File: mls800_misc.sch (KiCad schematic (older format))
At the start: 18 parts, among them SW2 SW_TACT_LED, SW3 SW_TACT_LED, SW4 SW_TACT_LED, SW5 SW_TACT_LED, SW6 SW_TACT_LED, SW7 SW_TACT_LED, SW8 SW_TACT_LED, SW9 SW_TACT_LED, U4 MCP23017

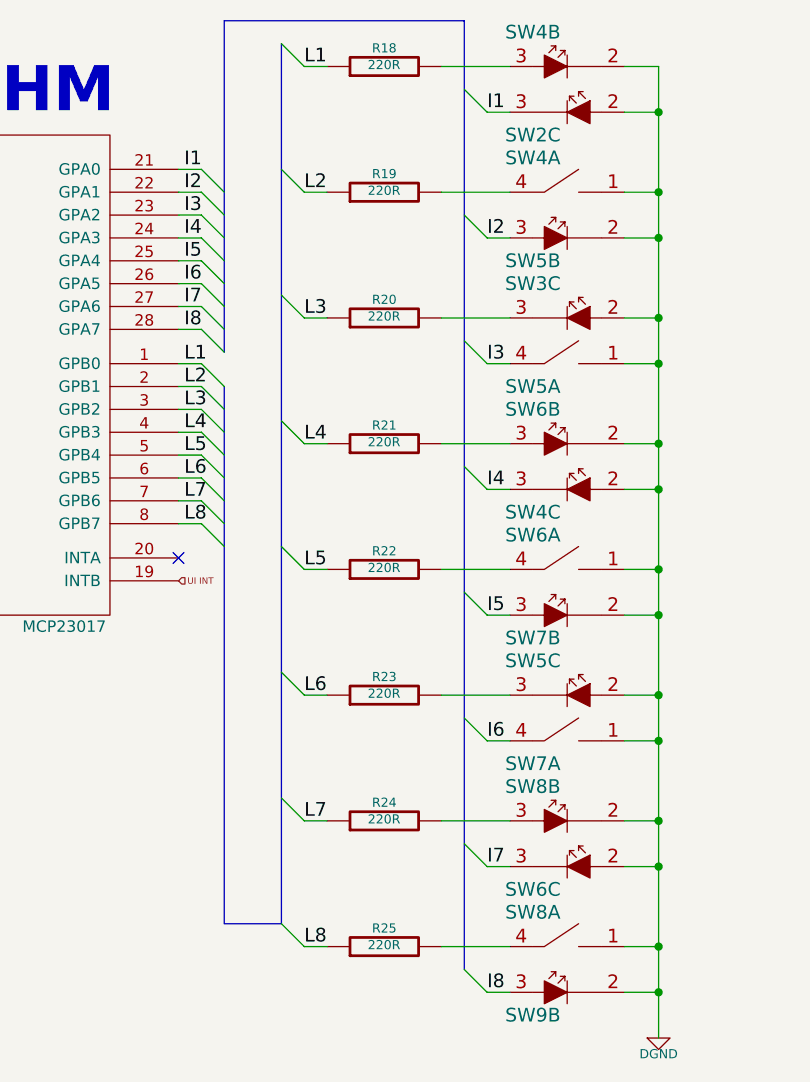
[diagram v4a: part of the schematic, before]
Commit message: MLS800 : disabled switch tact led "interchangeable" units => fixed annotations
MLS800 : fixed some erc errors in old "misc" sheet
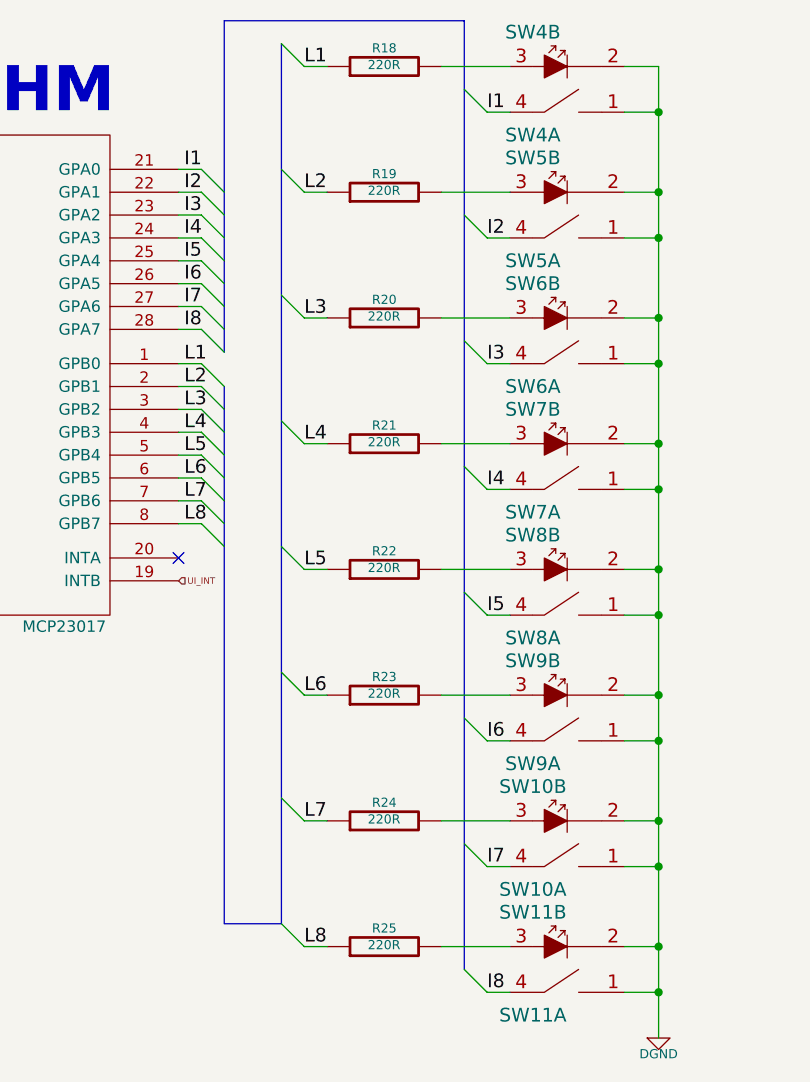
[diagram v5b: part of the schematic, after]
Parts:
- renumbered SW6 to SW10, SW8 to SW10, SW9 to SW11, SW8 to SW11, SW2 to SW4, SW4 to SW5, SW5 to SW6, SW3 to SW6, SW4 to SW7, SW6 to SW7, SW7 to SW8, SW6 to SW8, SW7 to SW9, SW5 to SW9
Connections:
- net DGND: now also SW10.1, SW11.1, SW11.2, SW4.1, SW5.1, SW5.2, SW7.1, SW8.1, SW8.2; no longer SW10.2, SW11.1, SW11.2, SW4.2, SW5.1, SW5.2, SW7.2, SW8.1, SW8.2
- net I1: now also SW4.4; no longer SW4.3
- net I2: now also SW5.4; no longer SW5.3
- net I4: now also SW7.4; no longer SW7.3
- net I5: now also SW8.4; no longer SW8.3
- net I7: now also SW10.4; no longer SW10.3
- net I8: now also SW11.4; no longer SW11.3
- net at R19.2: now also SW5.3; no longer SW5.4
- net at R22.2: now also SW8.3; no longer SW8.4
- net at R25.2: now also SW11.3; no longer SW11.4
- net UI INT renamed UI_INT
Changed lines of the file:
@@
 $EndComp
 $Comp
-L VCC #PWR43
+L VCC #PWR045
 U 1 1 5350562C
 P 750 1500
-F 0 "#PWR43" H 750 1600 30  0001 C CNN
+F 0 "#PWR045" H 750 1600 30  0001 C CNN
 F 1 "VCC" H 750 1600 30  0000 C CNN
 F 2 "" H 750 1500 60  0000 C CNN
@@
 SCL
 Text HLabel 3150 3350 2    28   Input ~ 0
-UI INT
+UI_INT
 NoConn ~ 3150 3250
 Entry Wire Line
@@
 	3600 4850 3700 4950
 $Comp
-L SW_TACT_LED SW2
-U 3 1 53B9BB32
+L SW_TACT_LED SW4
+U 1 1 53B9BB32
 P 4900 1300
-F 0 "SW2" H 4700 1200 60  0000 C CNN
+F 0 "SW4" H 4700 1200 60  0000 C CNN
 F 1 "SW_TACT_LED" H 4950 1200 60  0001 C CNN
 F 2 "" H 4900 1300 60  0000 C CNN
 F 3 "" H 4900 1300 60  0000 C CNN
-	3    4900 1300
+	1    4900 1300
 	1    0    0    -1
 $EndComp
@@
 $Comp
 L SW_TACT_LED SW5
-U 2 1 53B9BB96
+U 1 1 53B9BB96
 P 4900 1850
 F 0 "SW5" H 4700 1750 60  0000 C CNN
@@
 F 2 "" H 4900 1850 60  0000 C CNN
 F 3 "" H 4900 1850 60  0000 C CNN
-	2    4900 1850
-	1    0    0    -1
-$EndComp
-$Comp
-L SW_TACT_LED SW4
-U 1 1 53B9BB9C
+	1    4900 1850
+	1    0    0    -1
+$EndComp
+$Comp
+L SW_TACT_LED SW5
+U 2 1 53B9BB9C
 P 4900 1650
-F 0 "SW4" H 4700 1800 60  0000 C CNN
+F 0 "SW5" H 4700 1800 60  0000 C CNN
 F 1 "SW_TACT_LED" H 4950 1550 60  0001 C CNN
 F 2 "" H 4900 1650 60  0000 C CNN
 F 3 "" H 4900 1650 60  0000 C CNN
-	1    4900 1650
-	1    0    0    -1
-$EndComp
-$Comp
-L SW_TACT_LED SW5
+	2    4900 1650
+	1    0    0    -1
+$EndComp
+$Comp
+L SW_TACT_LED SW6
 U 1 1 53B9BBAC
 P 4900 2400
-F 0 "SW5" H 4700 2300 60  0000 C CNN
+F 0 "SW6" H 4700 2300 60  0000 C CNN
 F 1 "SW_TACT_LED" H 4950 2300 60  0001 C CNN
 F 2 "" H 4900 2400 60  0000 C CNN
@@
 $EndComp
 $Comp
-L SW_TACT_LED SW3
-U 3 1 53B9BBB2
+L SW_TACT_LED SW6
+U 2 1 53B9BBB2
 P 4900 2200
-F 0 "SW3" H 4700 2350 60  0000 C CNN
+F 0 "SW6" H 4700 2350 60  0000 C CNN
 F 1 "SW_TACT_LED" H 4950 2100 60  0001 C CNN
 F 2 "" H 4900 2200 60  0000 C CNN
 F 3 "" H 4900 2200 60  0000 C CNN
-	3    4900 2200
-	1    0    0    -1
-$EndComp
-$Comp
-L SW_TACT_LED SW4
-U 3 1 53B9BBB8
+	2    4900 2200
+	1    0    0    -1
+$EndComp
+$Comp
+L SW_TACT_LED SW7
+U 1 1 53B9BBB8
 P 4900 2950
-F 0 "SW4" H 4700 2850 60  0000 C CNN
+F 0 "SW7" H 4700 2850 60  0000 C CNN
 F 1 "SW_TACT_LED" H 4950 2850 60  0001 C CNN
 F 2 "" H 4900 2950 60  0000 C CNN
 F 3 "" H 4900 2950 60  0000 C CNN
-	3    4900 2950
-	1    0    0    -1
-$EndComp
-$Comp
-L SW_TACT_LED SW6
+	1    4900 2950
+	1    0    0    -1
+$EndComp
+$Comp
+L SW_TACT_LED SW7
 U 2 1 53B9BBBE
 P 4900 2750
-F 0 "SW6" H 4700 2900 60  0000 C CNN
+F 0 "SW7" H 4700 2900 60  0000 C CNN
 F 1 "SW_TACT_LED" H 4950 2650 60  0001 C CNN
 F 2 "" H 4900 2750 60  0000 C CNN
@@
 $EndComp
 $Comp
-L SW_TACT_LED SW7
-U 2 1 53B9BBC4
+L SW_TACT_LED SW8
+U 1 1 53B9BBC4
 P 4900 3500
-F 0 "SW7" H 4700 3400 60  0000 C CNN
+F 0 "SW8" H 4700 3400 60  0000 C CNN
 F 1 "SW_TACT_LED" H 4950 3400 60  0001 C CNN
 F 2 "" H 4900 3500 60  0000 C CNN
 F 3 "" H 4900 3500 60  0000 C CNN
-	2    4900 3500
-	1    0    0    -1
-$EndComp
-$Comp
-L SW_TACT_LED SW6
-U 1 1 53B9BBCA
+	1    4900 3500
+	1    0    0    -1
+$EndComp
+$Comp
+L SW_TACT_LED SW8
+U 2 1 53B9BBCA
 P 4900 3300
-F 0 "SW6" H 4700 3450 60  0000 C CNN
+F 0 "SW8" H 4700 3450 60  0000 C CNN
 F 1 "SW_TACT_LED" H 4950 3200 60  0001 C CNN
 F 2 "" H 4900 3300 60  0000 C CNN
 F 3 "" H 4900 3300 60  0000 C CNN
-	1    4900 3300
-	1    0    0    -1
-$EndComp
-$Comp
-L SW_TACT_LED SW7
+	2    4900 3300
+	1    0    0    -1
+$EndComp
+$Comp
+L SW_TACT_LED SW9
 U 1 1 53B9BBD0
 P 4900 4050
-F 0 "SW7" H 4700 3950 60  0000 C CNN
+F 0 "SW9" H 4700 3950 60  0000 C CNN
 F 1 "SW_TACT_LED" H 4950 3950 60  0001 C CNN
 F 2 "" H 4900 4050 60  0000 C CNN
@@
 $EndComp
 $Comp
-L SW_TACT_LED SW5
-U 3 1 53B9BBD6
+L SW_TACT_LED SW9
+U 2 1 53B9BBD6
 P 4900 3850
-F 0 "SW5" H 4700 4000 60  0000 C CNN
+F 0 "SW9" H 4700 4000 60  0000 C CNN
 F 1 "SW_TACT_LED" H 4950 3750 60  0001 C CNN
 F 2 "" H 4900 3850 60  0000 C CNN
 F 3 "" H 4900 3850 60  0000 C CNN
-	3    4900 3850
-	1    0    0    -1
-$EndComp
-$Comp
-L SW_TACT_LED SW6
-U 3 1 53B9BBDC
+	2    4900 3850
+	1    0    0    -1
+$EndComp
+$Comp
+L SW_TACT_LED SW10
+U 1 1 53B9BBDC
 P 4900 4600
-F 0 "SW6" H 4700 4500 60  0000 C CNN
+F 0 "SW10" H 4700 4500 60  0000 C CNN
 F 1 "SW_TACT_LED" H 4950 4500 60  0001 C CNN
 F 2 "" H 4900 4600 60  0000 C CNN
 F 3 "" H 4900 4600 60  0000 C CNN
-	3    4900 4600
-	1    0    0    -1
-$EndComp
-$Comp
-L SW_TACT_LED SW8
+	1    4900 4600
+	1    0    0    -1
+$EndComp
+$Comp
+L SW_TACT_LED SW10
 U 2 1 53B9BBE2
 P 4900 4400
-F 0 "SW8" H 4700 4550 60  0000 C CNN
+F 0 "SW10" H 4700 4550 60  0000 C CNN
 F 1 "SW_TACT_LED" H 4950 4300 60  0001 C CNN
 F 2 "" H 4900 4400 60  0000 C CNN
@@
 $EndComp
 $Comp
-L SW_TACT_LED SW9
-U 2 1 53B9BBE8
+L SW_TACT_LED SW11
+U 1 1 53B9BBE8
 P 4900 5150
-F 0 "SW9" H 4700 5050 60  0000 C CNN
+F 0 "SW11" H 4700 5050 60  0000 C CNN
 F 1 "SW_TACT_LED" H 4950 5050 60  0001 C CNN
 F 2 "" H 4900 5150 60  0000 C CNN
 F 3 "" H 4900 5150 60  0000 C CNN
-	2    4900 5150
-	1    0    0    -1
-$EndComp
-$Comp
-L SW_TACT_LED SW8
-U 1 1 53B9BBEE
+	1    4900 5150
+	1    0    0    -1
+$EndComp
+$Comp
+L SW_TACT_LED SW11
+U 2 1 53B9BBEE
 P 4900 4950
-F 0 "SW8" H 4700 5100 60  0000 C CNN
+F 0 "SW11" H 4700 5100 60  0000 C CNN
 F 1 "SW_TACT_LED" H 4950 4850 60  0001 C CNN
 F 2 "" H 4900 4950 60  0000 C CNN
 F 3 "" H 4900 4950 60  0000 C CNN
-	1    4900 4950
+	2    4900 4950
 	1    0    0    -1
 $EndComp
@@
 Connection ~ 5250 1300
 $Comp
-L DGND #PWR46
+L DGND #PWR046
 U 1 1 53F19F43
 P 5250 5350
-F 0 "#PWR46" H 5250 5350 40  0001 C CNN
+F 0 "#PWR046" H 5250 5350 40  0001 C CNN
 F 1 "DGND" H 5250 5280 40  0000 C CNN
 F 2 "" H 5250 5350 60  0000 C CNN
@@
 $EndComp
 $Comp
-L DGND #PWR45
+L DGND #PWR047
 U 1 1 53F19F5C
 P 2200 3800
-F 0 "#PWR45" H 2200 3800 40  0001 C CNN
+F 0 "#PWR047" H 2200 3800 40  0001 C CNN
 F 1 "DGND" H 2200 3730 40  0000 C CNN
 F 2 "" H 2200 3800 60  0000 C CNN
@@
 $EndComp
 $Comp
-L DGND #PWR44
+L DGND #PWR048
 U 1 1 53F19F6B
 P 1100 2100
-F 0 "#PWR44" H 1100 2100 40  0001 C CNN
+F 0 "#PWR048" H 1100 2100 40  0001 C CNN
 F 1 "DGND" H 1100 2030 40  0000 C CNN
 F 2 "" H 1100 2100 60  0000 C CNN
